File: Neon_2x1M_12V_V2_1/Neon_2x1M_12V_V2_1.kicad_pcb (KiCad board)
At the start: 2 copper layers, 60 x 60 mm, 32 parts, among them J2 Barrel_Jack_MountingPin, J6 Conn_01x03_Pin, J7 Screw_Terminal_01x02, J8 Screw_Terminal_01x02, Q1 IRLML2502TRPBF, Q2 IRLML2502TRPBF, SW1 SW_Push, SW2 SW_Push, U1 ESP32-WROOM-32, U3 LM2596T-ADJ

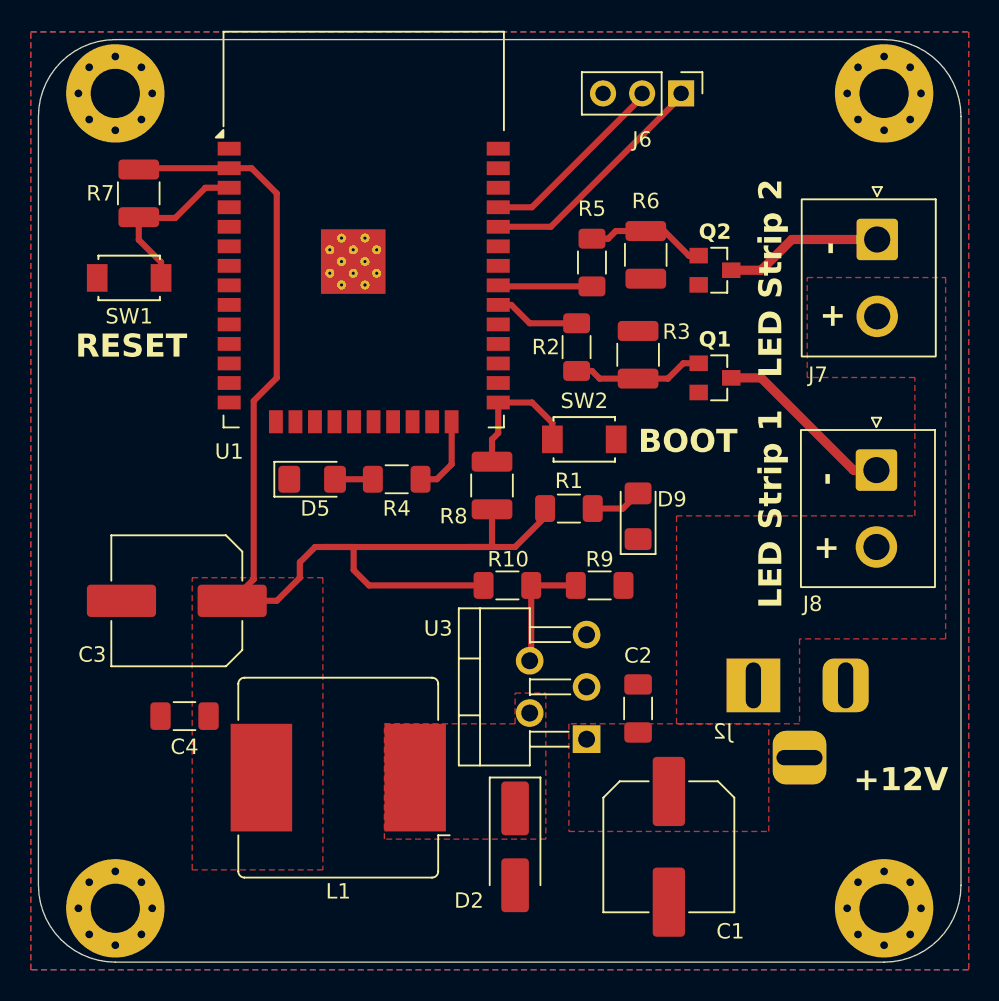
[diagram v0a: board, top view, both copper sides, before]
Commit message: updated PCB layout
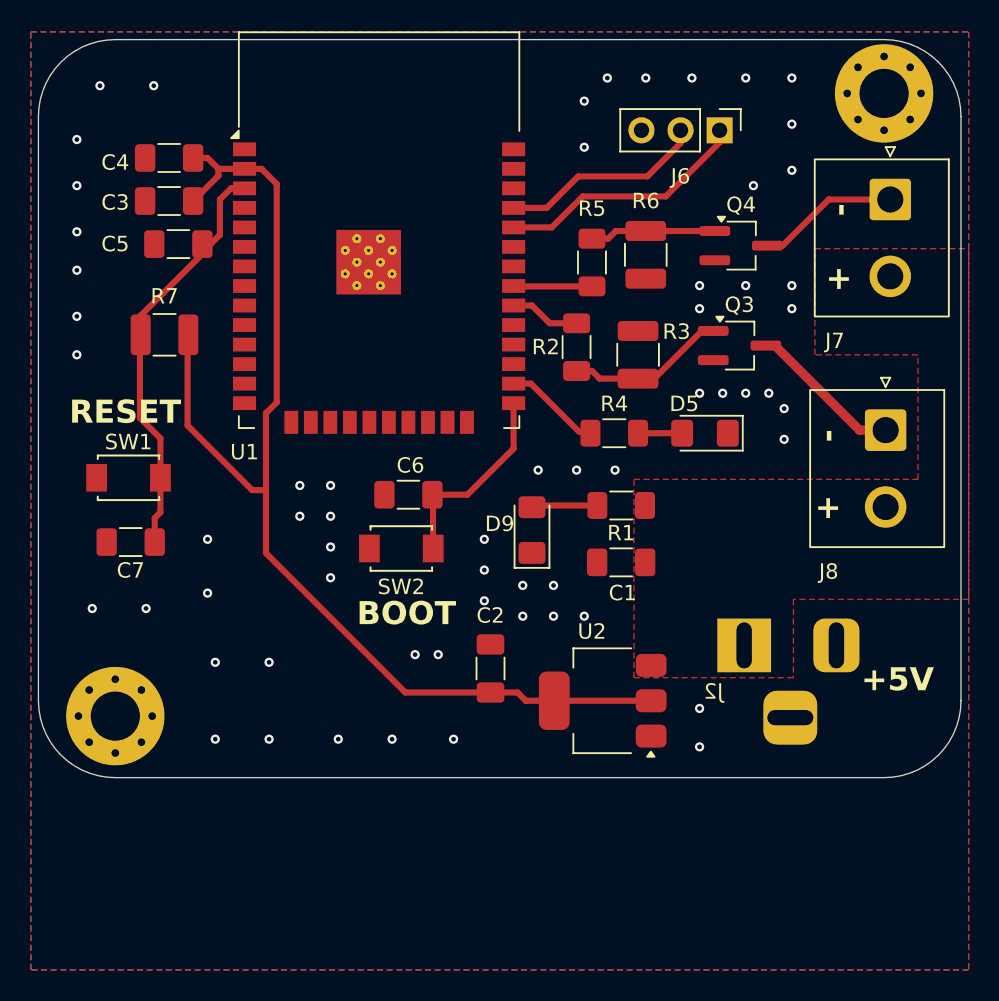
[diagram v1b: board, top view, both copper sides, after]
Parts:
- removed D2: SS34, Diode_SMD:D_SMA_Handsoldering
- removed H2, H3: MountingHole_Pad, MountingHole:MountingHole_3.2mm_M3_Pad_Via
- removed L1: 47uH, Inductor_SMD:L_Bourns_SRR1208_12.7x12.7mm
- removed Q1, Q2: IRLML2502TRPBF, custom_SOT23:custom_SOT23
- removed R10: 27K, Resistor_SMD:R_1206_3216Metric_Pad1.30x1.75mm_HandSolder
- removed R8: 10k Ohm, Resistor_SMD:R_1210_3225Metric_Pad1.30x2.65mm_HandSolder
- removed R9: 16K, Resistor_SMD:R_1206_3216Metric_Pad1.30x1.75mm_HandSolder
- removed U3: LM2596T-ADJ, Package_TO_SOT_THT:TO-220-5_P3.4x3.7mm_StaggerOdd_Lead3.8mm_Vertical
- added C5: 0.1uF/50V(10%), Capacitor_SMD:C_1206_3216Metric_Pad1.33x1.80mm_HandSolder, F.Cu at (168.6, 105.3)
- added C6: 0.1uF/50V(10%), Capacitor_SMD:C_1206_3216Metric_Pad1.33x1.80mm_HandSolder, F.Cu at (183.6, 121.6)
- added C7: 0.1uF/50V(10%), Capacitor_SMD:C_1206_3216Metric_Pad1.33x1.80mm_HandSolder, F.Cu at (165.5, 124.7)
- added Q3: AO3400A, Package_TO_SOT_SMD:TSOT-23_HandSoldering, F.Cu at (205.1, 111.9)
- added Q4: AO3400A, Package_TO_SOT_SMD:TSOT-23_HandSoldering, F.Cu at (205.2, 105.4)
- added U2: AMS1117-3.3, Package_TO_SOT_SMD:SOT-223-3_TabPin2, F.Cu at (196.2, 135.0)
- C1: value 100uF -> 22uF/10V(20%); footprint Capacitor_SMD:C_Elec_8x10.2 -> Capacitor_SMD:C_1206_3216Metric_Pad1.33x1.80mm_HandSolder
- C2: value 100nF -> 22uF/10V(20%)
- C3: value 220uF -> 22uF/10V(20%); footprint Capacitor_SMD:C_Elec_8x10.2 -> Capacitor_SMD:C_1206_3216Metric_Pad1.33x1.80mm_HandSolder
- C4: value 100nF -> 0.1uF/50V(10%)
- R1: value 820 Ohm -> 2K(5%)
- R3, R6, R7: value 10k Ohm -> 10k
- R4: value 820 Ohm -> 1K
- moved C4 36.3 mm to (168.0, 99.7)
- moved C3 26.0 mm to (168.0, 102.5)
- moved D5 25.7 mm to (202.8, 117.6), turned to 180 degrees
- moved C1 18.8 mm to (197.4, 126.0), turned to 180 degrees
- moved R4 14.5 mm to (196.9, 117.6), turned to 180 degrees
- moved SW2 13.9 mm to (183.1, 125.1), turned to 0 degrees
- moved SW1 13.0 mm to (165.4, 120.5)
- moved H1 12.5 mm to (164.5, 136.0)
- moved C2 9.95 mm to (188.9, 132.9)
- moved R7 9.35 mm to (167.7, 111.2), turned to 180 degrees
- moved D9 6.96 mm to (191.6, 123.9)
- moved J6 3.46 mm to (203.8, 97.9)
- moved R1 3.41 mm to (197.4, 122.3), turned to 0 degrees
- moved J7 2.74 mm to (214.9, 102.4)
- moved J2 2.67 mm to (205.4, 131.4)
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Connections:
- C1 pad 1: +12V -> +5V
- C2 pad 1: +12V -> +3V3
- J2 pad 1: +12V -> +5V
- J7 pad 2: +12V -> +5V
- J8 pad 2: +12V -> +5V
- R1 pad 2: +3V3 -> +5V
- R4 pad 2: ESP_IO2 -> ESP_IO4
- R7 pad 1: ESP_EN -> +3V3
- R7 pad 2: +3V3 -> ESP_EN
- U1 pad 10: ESP_IO25 -> unconnected-(U1-IO25-Pad10)
- U1 pad 11: ESP_IO26 -> unconnected-(U1-IO26-Pad11)
- U1 pad 12: ESP_IO27 -> unconnected-(U1-IO27-Pad12)
- U1 pad 13: ESP_IO14 -> unconnected-(U1-IO14-Pad13)
- U1 pad 14: ESP_IO12 -> unconnected-(U1-IO12-Pad14)
- U1 pad 16: ESP_IO13 -> unconnected-(U1-IO13-Pad16)
- U1 pad 23: ESP_IO15 -> unconnected-(U1-IO15-Pad23)
- U1 pad 24: ESP_IO2 -> unconnected-(U1-IO2-Pad24)
- U1 pad 27: ESP_IO16 -> unconnected-(U1-IO16-Pad27)
- U1 pad 28: ESP_IO17 -> unconnected-(U1-IO17-Pad28)
- U1 pad 29: ESP_IO5 -> unconnected-(U1-IO5-Pad29)
- U1 pad 33: ESP_IO21 -> unconnected-(U1-IO21-Pad33)
- U1 pad 36: ESP_IO22 -> unconnected-(U1-IO22-Pad36)
- U1 pad 37: ESP_IO23 -> unconnected-(U1-IO23-Pad37)
- U1 pad 4: ESP_SVP -> unconnected-(U1-SENSOR_VP-Pad4)
- U1 pad 5: ESP_SVN -> unconnected-(U1-SENSOR_VN-Pad5)
- U1 pad 6: ESP_IO34 -> unconnected-(U1-IO34-Pad6)
- U1 pad 7: ESP_IO35 -> unconnected-(U1-IO35-Pad7)
- U1 pad 8: ESP_IO32 -> unconnected-(U1-IO32-Pad8)
- U1 pad 9: ESP_IO33 -> unconnected-(U1-IO33-Pad9)
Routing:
- net ESP_EN: track 11.3 -> 27.4 mm
- net Net-(U3-FB): track 7.84 -> 0.00 mm
- net ESP_IO4: track 0.00 -> 6.33 mm
- net ESP_IO2: track 5.20 -> 0.00 mm
- net ESP_IO0: track 9.15 -> 13.0 mm
- net +3V3: track 77.7 -> 75.0 mm
- net B_Jack: track 11.9 -> 10.1 mm
- net Net-(Q3-G): track 8.56 -> 10.4 mm
- net P_Jack: track 10.3 -> 9.23 mm
- net ESP_IO19: track 6.12 -> 5.11 mm
- net ESP_IO18: track 5.59 -> 4.57 mm
- net ESP_U0RX: track 15.6 -> 16.6 mm
- net Net-(D9-A): track 3.36 -> 4.30 mm
- net ESP_U0TX: track 12.6 -> 13.4 mm
- net GND: vias 0 -> 61
- added copper zone on F.Cu, net +5V
- removed copper zone on F.Cu, net +12V
- removed copper zone on F.Cu, net +3V3
- removed copper zone on F.Cu, net /BUCK_SW
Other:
- board size 60 x 60 mm -> 60 x 48 mm
- board text added: "+5V"
- board text removed: "+12V"
- board text removed: "LED Strip 1"
- board text removed: "LED Strip 2"
